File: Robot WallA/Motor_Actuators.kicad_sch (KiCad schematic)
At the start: 54 parts, among them IC9 74LVC2G241DP-Q100H, J19 22-03-5035, J20 22-03-5035, J21 22-03-5035, J22 22-03-5035, J23 Conn_01x03, J24 281695-3, J25 Conn_01x03, J26 281695-3, J27 Conn_01x03, J28 281695-3, J29 Conn_01x03, J30 39501-1002, J31 39501-1002, J32 Conn_01x03, J33 281695-3, Q4 BSS119, Q5 BSS119, U6 L298N

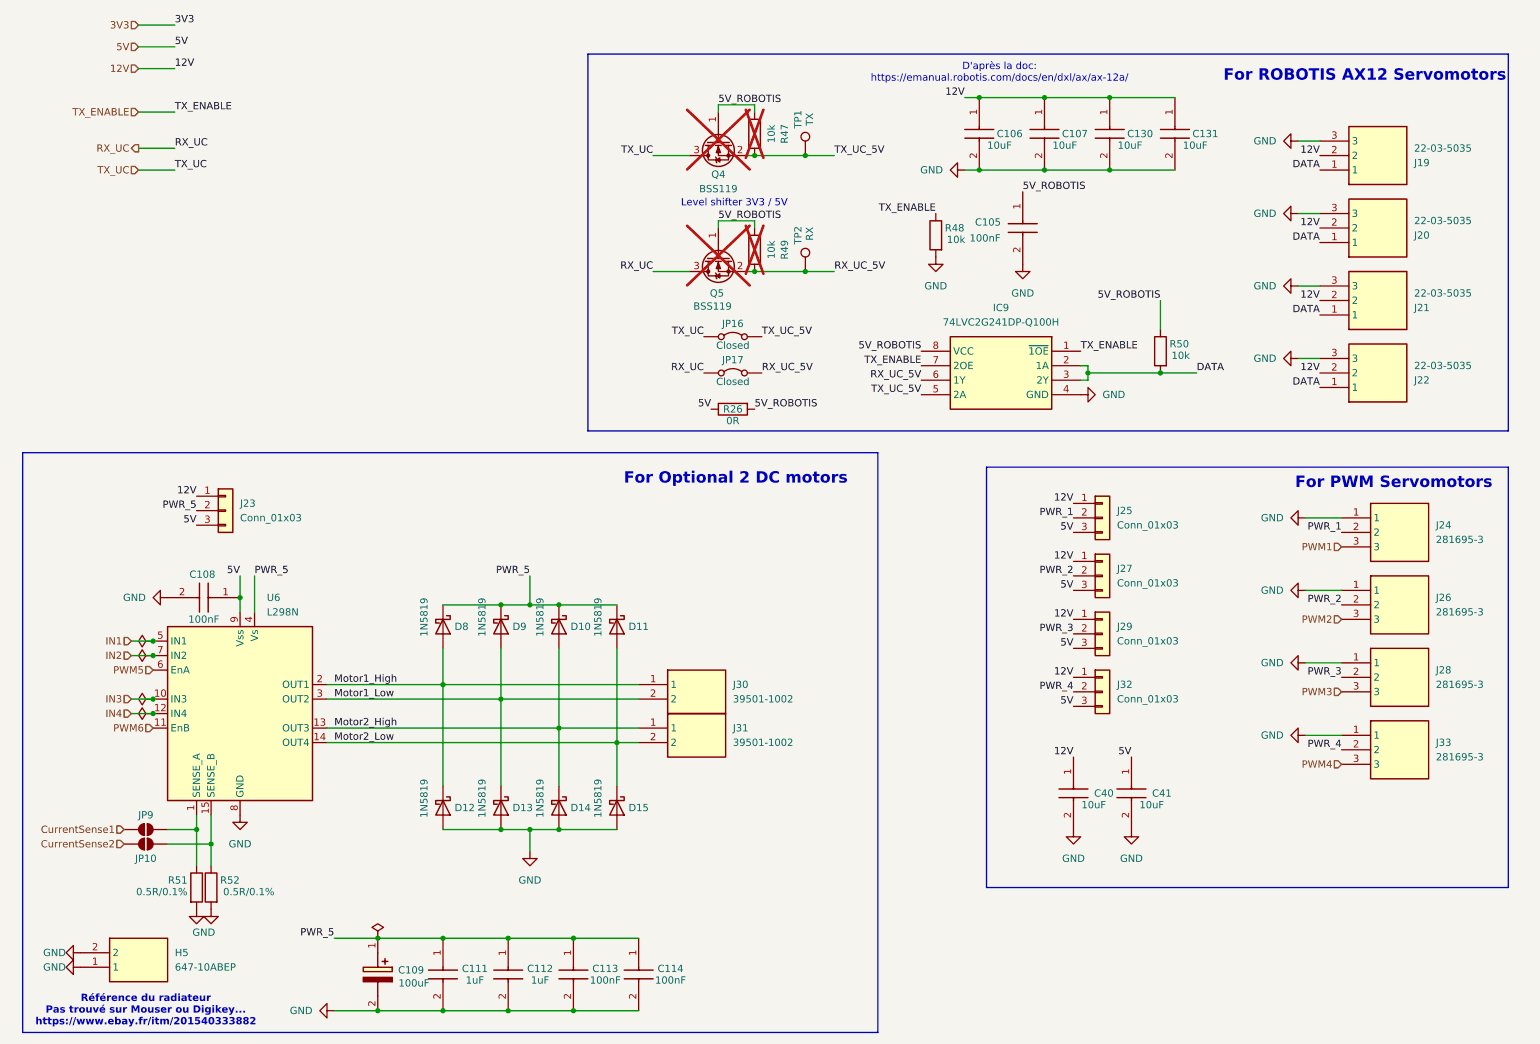
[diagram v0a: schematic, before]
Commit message: Added to BOM connectors and socket
Updated fab files
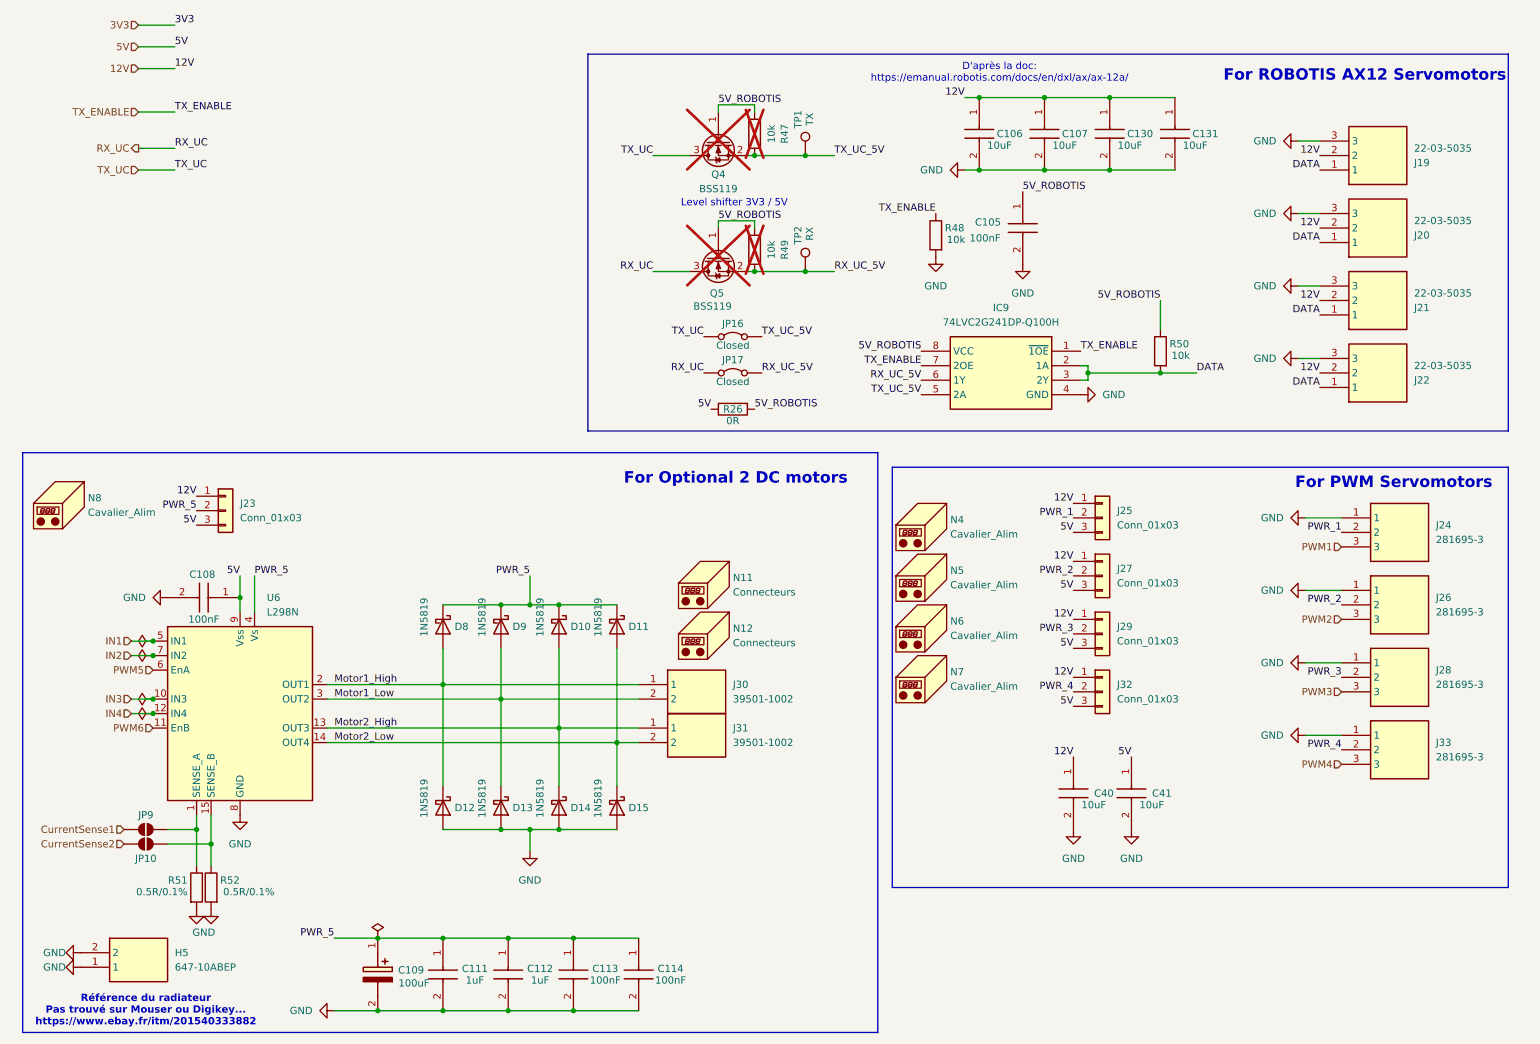
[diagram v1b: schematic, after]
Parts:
- added N11, N12: Connecteurs, symbol Mechanical:Housing
- added N4, N5, N6, N7, N8: Cavalier_Alim, symbol Mechanical:Housing

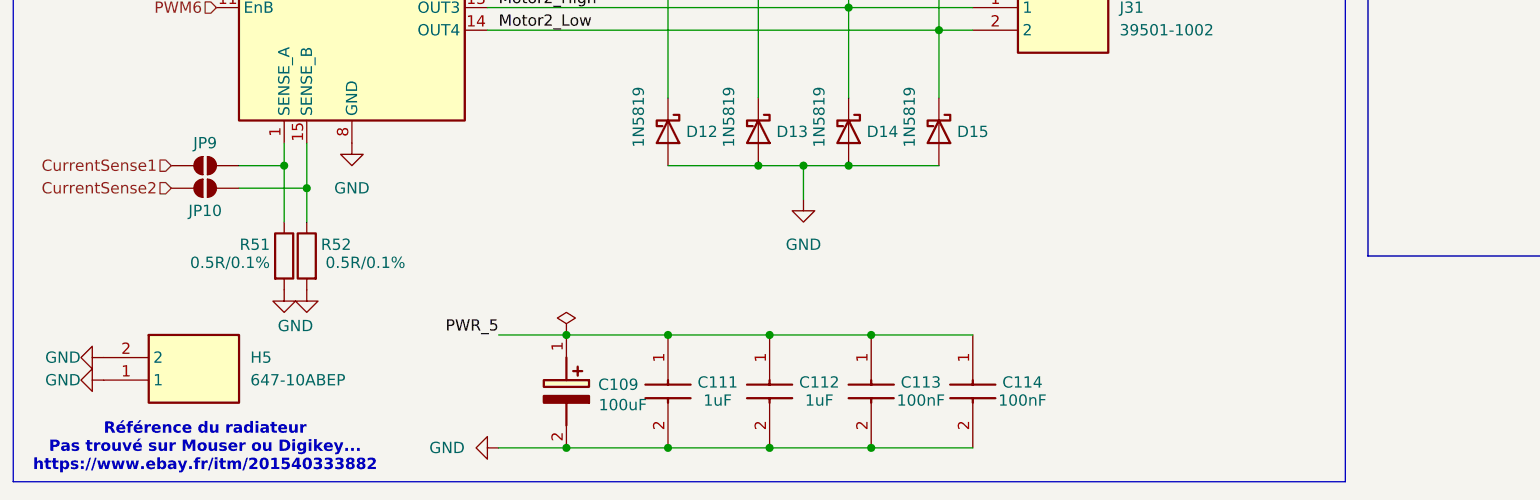
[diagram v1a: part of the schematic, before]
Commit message: Added 3 thermistor to measure temperature near 12V and 24V power supplies and near motor drivers
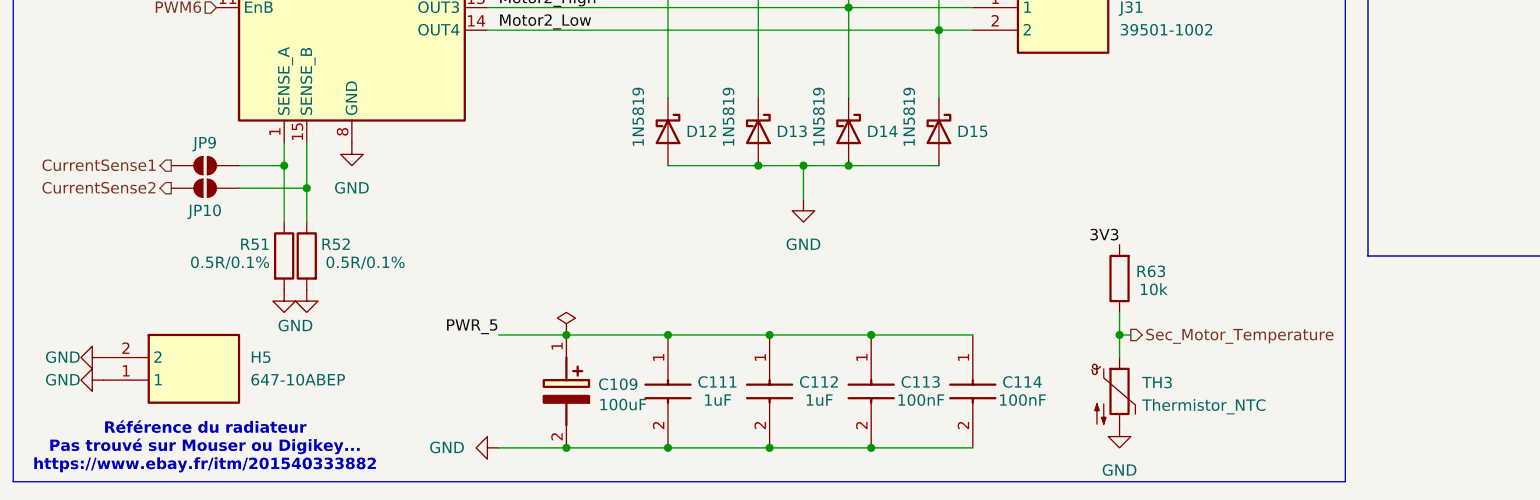
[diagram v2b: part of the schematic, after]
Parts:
- added R63: 10k, Resistor_SMD:R_0603_1608Metric_Pad0.98x0.95mm_HandSolder, symbol Device:R
- added TH3: Thermistor_NTC, Resistor_SMD:R_0603_1608Metric_Pad0.98x0.95mm_HandSolder, symbol Device:Thermistor_NTC
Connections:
- net 3V3: now also R63.2
- net GND: now also TH3.2
- new net Sec_Motor_Temperature: R63.1, TH3.1

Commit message: Modified footprint to simplify BOM. Finalized BOM.
Updated fab files
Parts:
- C105, C108, C113, C114: Manufacturer_Part_Number (none) -> KGM15BR71H104KT
- C106, C107, C130, C131, C40, C41: Manufacturer_Part_Number (none) -> CL10A106MA8NRNC
- C111, C112: value 1uF -> 1uF/50V; Manufacturer_Part_Number (none) -> CL10A105KB8NNNC
- IC9: value 74LVC2G241DP-Q100H -> 74LVC2G241DP_125; Manufacturer_Part_Number 74LVC2G241DP-Q100H -> 74LVC2G241DP_125
- J19, J20, J21, J22: Manufacturer_Part_Number 22-03-5035 -> '22-03-5035
- J23, J25, J27, J29, J32, JP16, JP17, R26: now left out of the parts list
- R47, R48, R49, R50, R63: Manufacturer_Part_Number (none) -> 667-ERJ-3GEYJ103V
- R51, R52: Manufacturer_Part_Number (none) -> CSR0603FKR500

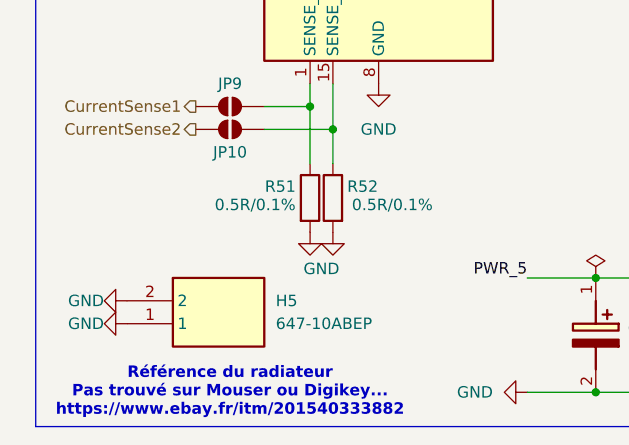
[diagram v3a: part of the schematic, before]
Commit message: Added Thermal pads for heatsinks in BOM.
Updated fab files
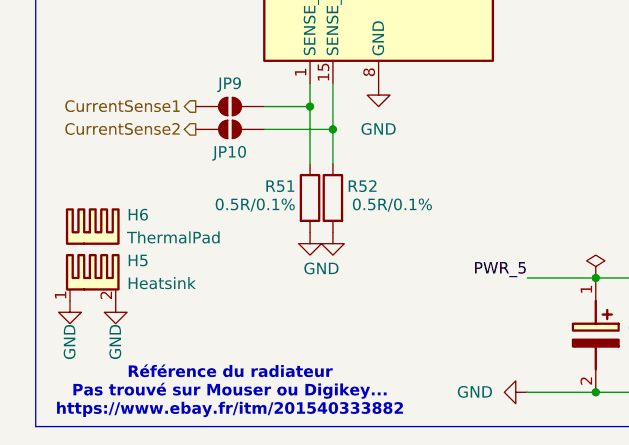
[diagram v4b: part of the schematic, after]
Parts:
- removed H5: 647-10ABEP, SamacSys_Parts:64710ABEP, symbol SamacSys_new:647-10ABEP
- added H5: Heatsink, SamacSys_Parts:64710ABEP, symbol Mechanical:Heatsink_Pad_2Pin
- added H6: ThermalPad, symbol Mechanical:Heatsink
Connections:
- net GND: now also H5.1, H5.2

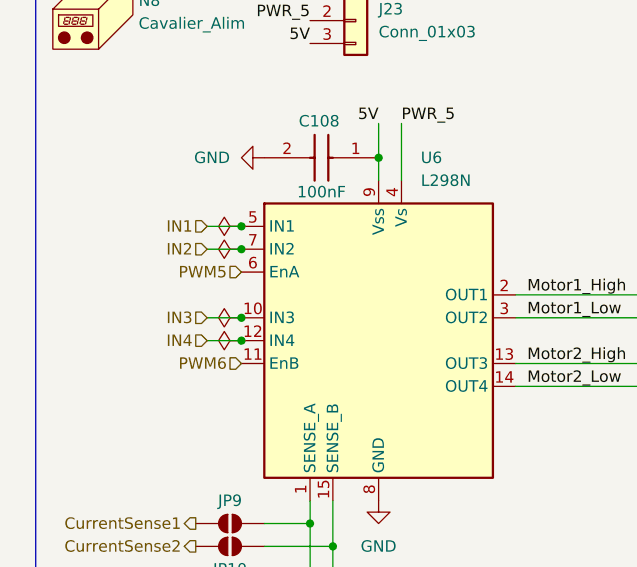
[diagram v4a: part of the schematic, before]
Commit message: Corrected schematic labels encoders according to PCB labels... (inversion...)
Add fab files
cleaned
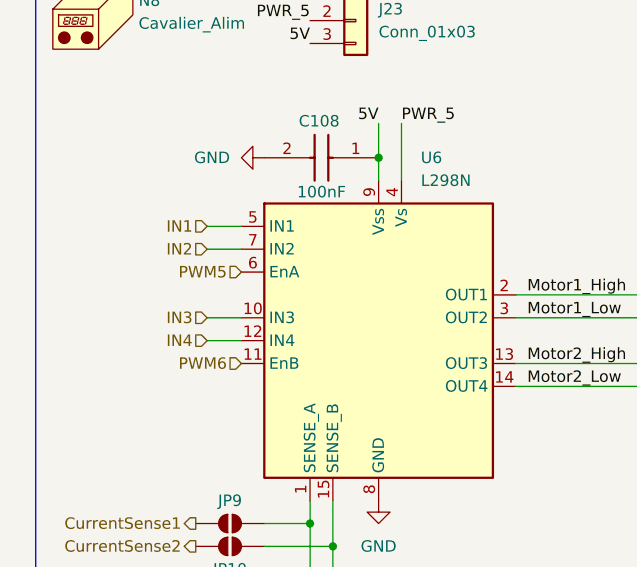
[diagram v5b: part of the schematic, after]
